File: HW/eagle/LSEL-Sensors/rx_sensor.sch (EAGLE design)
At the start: 14 parts, among them U1 Tiny45-20-SMT

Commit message: Documents
datasheets, RJ information
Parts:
- JP2: value (none) -> RJ11-2L-B; device SparkFun-Connectors:M04JST-PTH -> con-tycoelectronics:RJ11-2L-B
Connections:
- net GND: now also JP2.3; no longer JP2.2
- net SCL: now also JP2.2; no longer JP2.1
- net SDA/MOSI: now also JP2.5; no longer JP2.4
- net VCC: now also JP2.4; no longer JP2.3
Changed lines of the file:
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@@
 <part name="C2" library="SparkFun-Capacitors" deviceset="CAP" device="0603-CAP" value="100n"/>
 <part name="JP1" library="SparkFun-Connectors" deviceset="M04" device="JST-PTH"/>
-<part name="JP2" library="SparkFun-Connectors" deviceset="M04" device="JST-PTH"/>
+<part name="JP2" library="con-tycoelectronics" deviceset="RJ11" device="" technology="-2L-B" value="RJ11-2L-B"/>
 <part name="JP3" library="pinhead" deviceset="PINHD-2X3" device=""/>
 <part name="LED1" library="SparkFun-LED" deviceset="LED" device="0603"/>
@@
 </segment>
 <segment>
-<pinref part="JP2" gate="G$1" pin="3"/>
+<pinref part="JP2" gate="G$1" pin="4"/>
 <pinref part="JP1" gate="G$1" pin="2"/>
-<wire x1="71.12" y1="66.04" x2="50.8" y2="68.58" width="0.1524" layer="91"/>
+<wire x1="78.74" y1="71.12" x2="50.8" y2="68.58" width="0.1524" layer="91"/>
 <label x="58.42" y="68.58" size="1.778" layer="95"/>
 </segment>
@@
 <segment>
 <pinref part="JP1" gate="G$1" pin="3"/>
-<pinref part="JP2" gate="G$1" pin="2"/>
-<wire x1="50.8" y1="66.04" x2="71.12" y2="68.58" width="0.1524" layer="91"/>
+<pinref part="JP2" gate="G$1" pin="3"/>
+<wire x1="50.8" y1="66.04" x2="78.74" y2="68.58" width="0.1524" layer="91"/>
 <label x="58.42" y="66.04" size="1.778" layer="95"/>
 </segment>
@@
 </segment>
 <segment>
-<pinref part="JP2" gate="G$1" pin="1"/>
+<pinref part="JP2" gate="G$1" pin="2"/>
 <pinref part="JP1" gate="G$1" pin="4"/>
-<wire x1="71.12" y1="71.12" x2="50.8" y2="63.5" width="0.1524" layer="91"/>
+<wire x1="78.74" y1="66.04" x2="50.8" y2="63.5" width="0.1524" layer="91"/>
 <label x="58.42" y="63.5" size="1.778" layer="95"/>
 </segment>
@@
 <segment>
 <pinref part="JP1" gate="G$1" pin="1"/>
-<pinref part="JP2" gate="G$1" pin="4"/>
-<wire x1="50.8" y1="71.12" x2="71.12" y2="63.5" width="0.1524" layer="91"/>
+<pinref part="JP2" gate="G$1" pin="5"/>
+<wire x1="50.8" y1="71.12" x2="78.74" y2="73.66" width="0.1524" layer="91"/>
 <label x="58.42" y="71.12" size="1.778" layer="95"/>
 </segment>

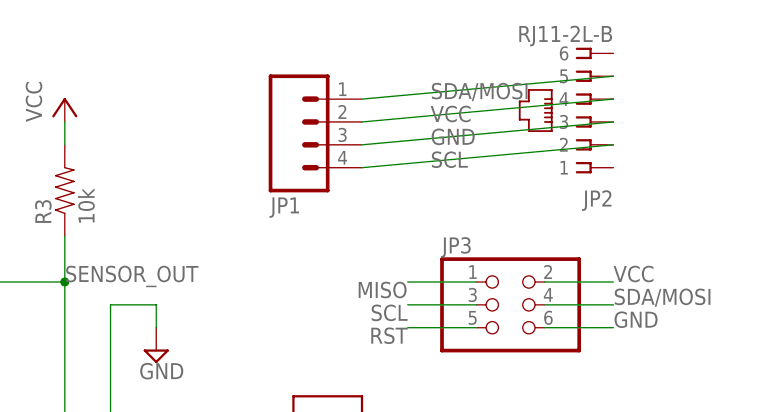
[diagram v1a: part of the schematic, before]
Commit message: Sensor RJ
Sensor connectors changed
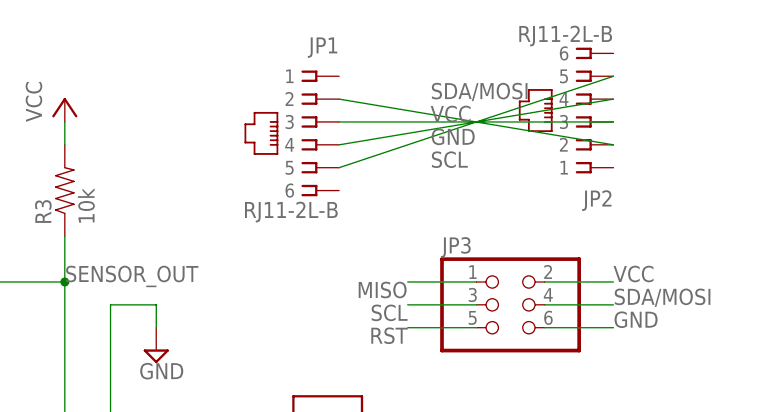
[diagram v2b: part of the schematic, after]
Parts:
- JP1: value (none) -> RJ11-2L-B; device SparkFun-Connectors:M04JST-PTH -> con-tycoelectronics:RJ11-2L-B
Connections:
- net SCL: now also JP1.2; no longer JP1.4
- net SDA/MOSI: now also JP1.5; no longer JP1.1
- net VCC: now also JP1.4; no longer JP1.2
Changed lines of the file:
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@@
 <?xml version="1.0" encoding="utf-8"?>
 <!DOCTYPE eagle SYSTEM "eagle.dtd">
-<eagle version="7.3.0">
+<eagle version="7.2.0">
 <drawing>
 <settings>
@@
 <part name="C1" library="SparkFun-Capacitors" deviceset="CAP" device="0603-CAP" value="100n"/>
 <part name="C2" library="SparkFun-Capacitors" deviceset="CAP" device="0603-CAP" value="100n"/>
-<part name="JP1" library="SparkFun-Connectors" deviceset="M04" device="JST-PTH"/>
+<part name="JP1" library="con-tycoelectronics" deviceset="RJ11" device="" technology="-2L-B"/>
 <part name="JP2" library="con-tycoelectronics" deviceset="RJ11" device="" technology="-2L-B" value="RJ11-2L-B"/>
 <part name="JP3" library="pinhead" deviceset="PINHD-2X3" device=""/>
@@
 <instance part="C1" gate="G$1" x="-76.2" y="48.26" rot="R180"/>
 <instance part="C2" gate="G$1" x="22.86" y="25.4" rot="R180"/>
-<instance part="JP1" gate="G$1" x="45.72" y="68.58" rot="MR180"/>
+<instance part="JP1" gate="G$1" x="45.72" y="68.58" rot="MR0"/>
 <instance part="JP2" gate="G$1" x="76.2" y="68.58" rot="R180"/>
 <instance part="JP3" gate="A" x="66.04" y="48.26"/>
@@
 <segment>
 <pinref part="JP2" gate="G$1" pin="4"/>
-<pinref part="JP1" gate="G$1" pin="2"/>
-<wire x1="78.74" y1="71.12" x2="50.8" y2="68.58" width="0.1524" layer="91"/>
+<pinref part="JP1" gate="G$1" pin="4"/>
+<wire x1="78.74" y1="71.12" x2="48.26" y2="66.04" width="0.1524" layer="91"/>
 <label x="58.42" y="68.58" size="1.778" layer="95"/>
 </segment>
@@
 <pinref part="JP1" gate="G$1" pin="3"/>
 <pinref part="JP2" gate="G$1" pin="3"/>
-<wire x1="50.8" y1="66.04" x2="78.74" y2="68.58" width="0.1524" layer="91"/>
+<wire x1="48.26" y1="68.58" x2="78.74" y2="68.58" width="0.1524" layer="91"/>
 <label x="58.42" y="66.04" size="1.778" layer="95"/>
 </segment>
@@
 <segment>
 <pinref part="JP2" gate="G$1" pin="2"/>
-<pinref part="JP1" gate="G$1" pin="4"/>
-<wire x1="78.74" y1="66.04" x2="50.8" y2="63.5" width="0.1524" layer="91"/>
+<pinref part="JP1" gate="G$1" pin="2"/>
+<wire x1="78.74" y1="66.04" x2="48.26" y2="71.12" width="0.1524" layer="91"/>
 <label x="58.42" y="63.5" size="1.778" layer="95"/>
 </segment>
@@
 </segment>
 <segment>
-<pinref part="JP1" gate="G$1" pin="1"/>
+<pinref part="JP1" gate="G$1" pin="5"/>
 <pinref part="JP2" gate="G$1" pin="5"/>
-<wire x1="50.8" y1="71.12" x2="78.74" y2="73.66" width="0.1524" layer="91"/>
+<wire x1="48.26" y1="63.5" x2="78.74" y2="73.66" width="0.1524" layer="91"/>
 <label x="58.42" y="71.12" size="1.778" layer="95"/>
 </segment>

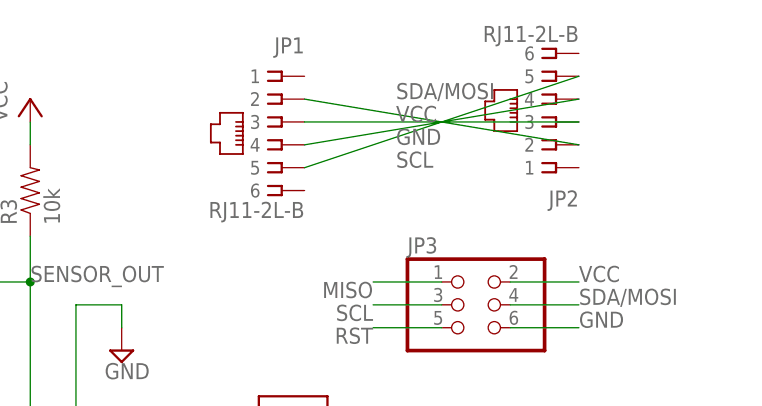
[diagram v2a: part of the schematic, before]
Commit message: Sensor IR
little changes
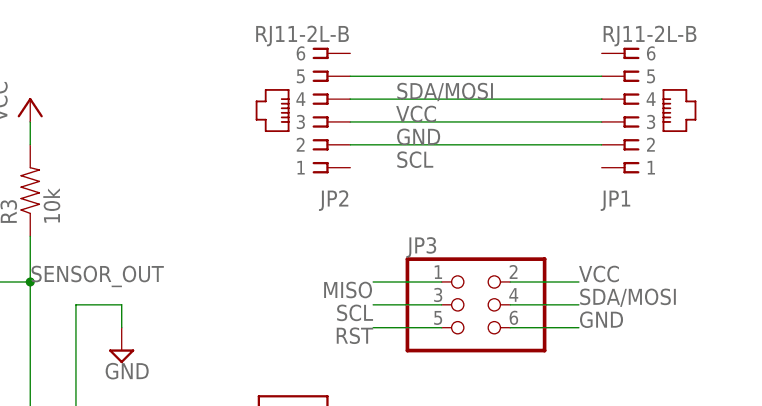
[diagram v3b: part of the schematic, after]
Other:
- moved on the sheet: JP1, JP2
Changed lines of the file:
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@@
 <instance part="C1" gate="G$1" x="-76.2" y="48.26" rot="R180"/>
 <instance part="C2" gate="G$1" x="22.86" y="25.4" rot="R180"/>
-<instance part="JP1" gate="G$1" x="45.72" y="68.58" rot="MR0"/>
-<instance part="JP2" gate="G$1" x="76.2" y="68.58" rot="R180"/>
+<instance part="JP1" gate="G$1" x="83.82" y="68.58" rot="MR180"/>
+<instance part="JP2" gate="G$1" x="50.8" y="68.58" rot="R180"/>
 <instance part="JP3" gate="A" x="66.04" y="48.26"/>
 <instance part="LED1" gate="G$1" x="-93.98" y="53.34"/>
@@
 <pinref part="JP2" gate="G$1" pin="4"/>
 <pinref part="JP1" gate="G$1" pin="4"/>
-<wire x1="78.74" y1="71.12" x2="48.26" y2="66.04" width="0.1524" layer="91"/>
+<wire x1="53.34" y1="71.12" x2="81.28" y2="71.12" width="0.1524" layer="91"/>
 <label x="58.42" y="68.58" size="1.778" layer="95"/>
 </segment>
@@
 <pinref part="JP1" gate="G$1" pin="3"/>
 <pinref part="JP2" gate="G$1" pin="3"/>
-<wire x1="48.26" y1="68.58" x2="78.74" y2="68.58" width="0.1524" layer="91"/>
+<wire x1="81.28" y1="68.58" x2="53.34" y2="68.58" width="0.1524" layer="91"/>
 <label x="58.42" y="66.04" size="1.778" layer="95"/>
 </segment>
@@
 <pinref part="JP2" gate="G$1" pin="2"/>
 <pinref part="JP1" gate="G$1" pin="2"/>
-<wire x1="78.74" y1="66.04" x2="48.26" y2="71.12" width="0.1524" layer="91"/>
+<wire x1="53.34" y1="66.04" x2="81.28" y2="66.04" width="0.1524" layer="91"/>
 <label x="58.42" y="63.5" size="1.778" layer="95"/>
 </segment>
@@
 <pinref part="JP1" gate="G$1" pin="5"/>
 <pinref part="JP2" gate="G$1" pin="5"/>
-<wire x1="48.26" y1="63.5" x2="78.74" y2="73.66" width="0.1524" layer="91"/>
+<wire x1="81.28" y1="73.66" x2="53.34" y2="73.66" width="0.1524" layer="91"/>
 <label x="58.42" y="71.12" size="1.778" layer="95"/>
 </segment>
